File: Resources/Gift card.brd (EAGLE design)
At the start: 76.2 x 25.1 mm, 27 parts, among them J1 USBSMD, J2 LPC_SWD_PINPROG, Q1 IRLML6402, Q2 IRLML2502SOT23, U1 LPC11U24FBD48/301, U2 MMA8452Q, U3 NCP551SN33T1G, U4 NCP551SN50T1G, Y1 SMDCRYSTAL

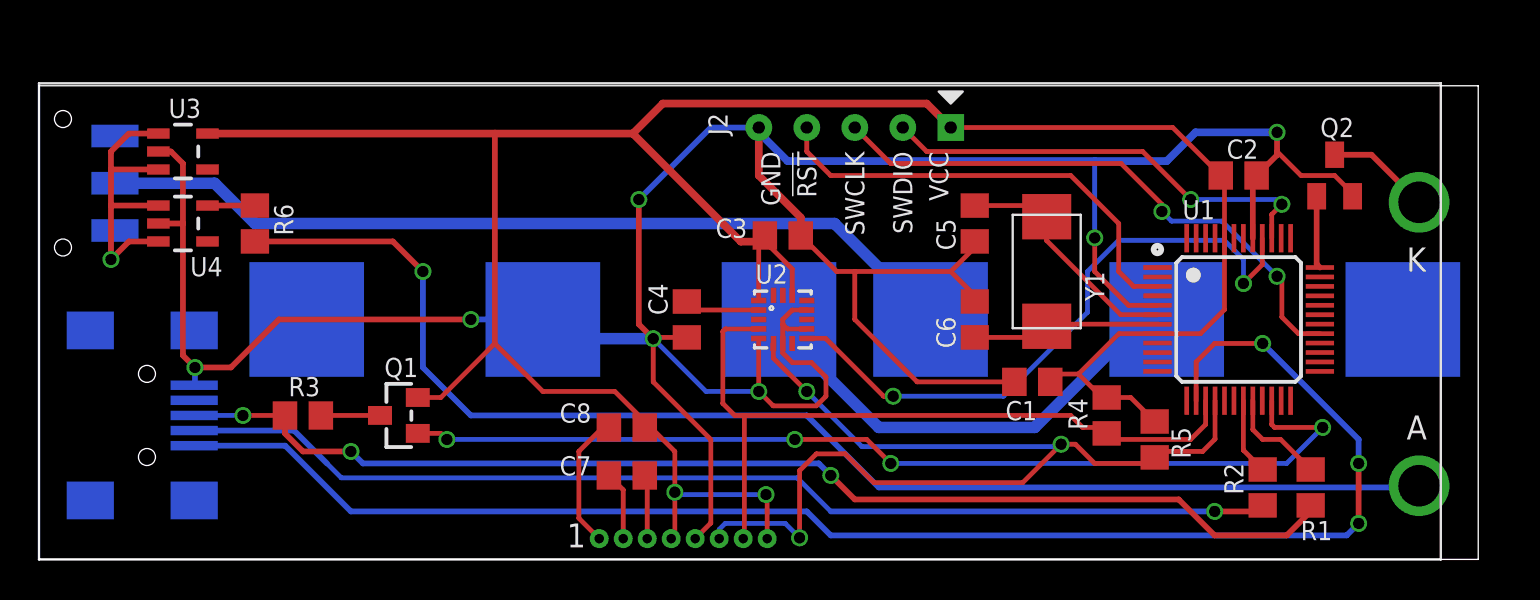
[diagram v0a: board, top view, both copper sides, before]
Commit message: Added drawable: hole; refactored abstraction error to #define
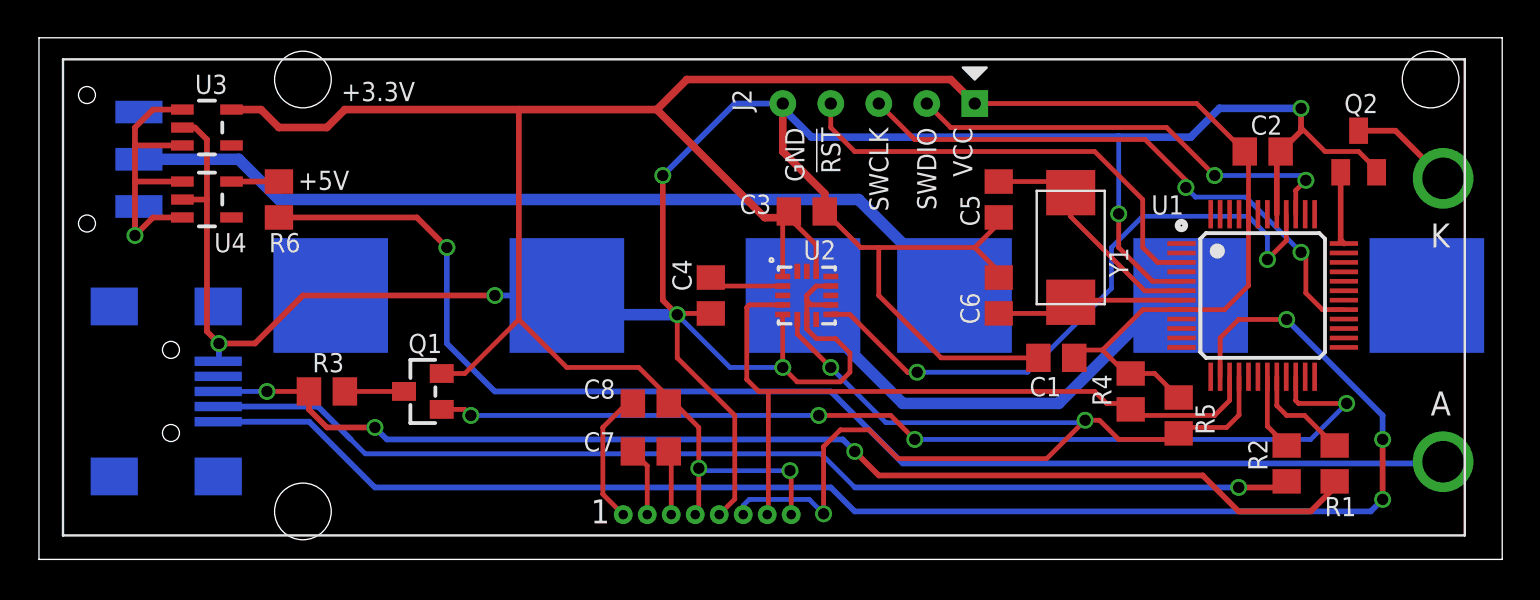
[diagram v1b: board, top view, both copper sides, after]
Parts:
- moved R2 1.80 mm to (66.0, 5.08)
- moved BT2 1.80 mm to (61.0, 14.0)
- moved C4 1.80 mm to (35.6, 14.0)
- moved U2 1.80 mm to (40.6, 14.0)
- moved R5 1.80 mm to (60.3, 7.62)
- moved C3 1.80 mm to (40.6, 18.4)
- moved J2 1.80 mm to (44.5, 24.1)
- moved J1 1.80 mm to (6.99, 8.89)
- moved BT1 1.80 mm to (27.9, 14.0)
- moved DS1 1.80 mm to (1.27, 1.27)
- moved C8 1.80 mm to (32.4, 8.26)
- moved Q1 1.80 mm to (20.3, 8.89)
- moved R3 1.80 mm to (15.2, 8.89)
- moved S1 1.80 mm to (2.54, 17.8)
- moved U3 1.80 mm to (8.89, 22.9)
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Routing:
- net 3V3: track 135.9 -> 136.7 mm
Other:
- board size 76.2 x 25.1 mm -> 77.5 x 27.6 mm
- board text added: "+3.3V"
- board text added: "+5V"
- board text added: "JWJ #2014-001"
- board text removed: "#2014-001"

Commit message: Fixed MR270 rotations for texts; fixed problem with non-attribute texts not being drawn
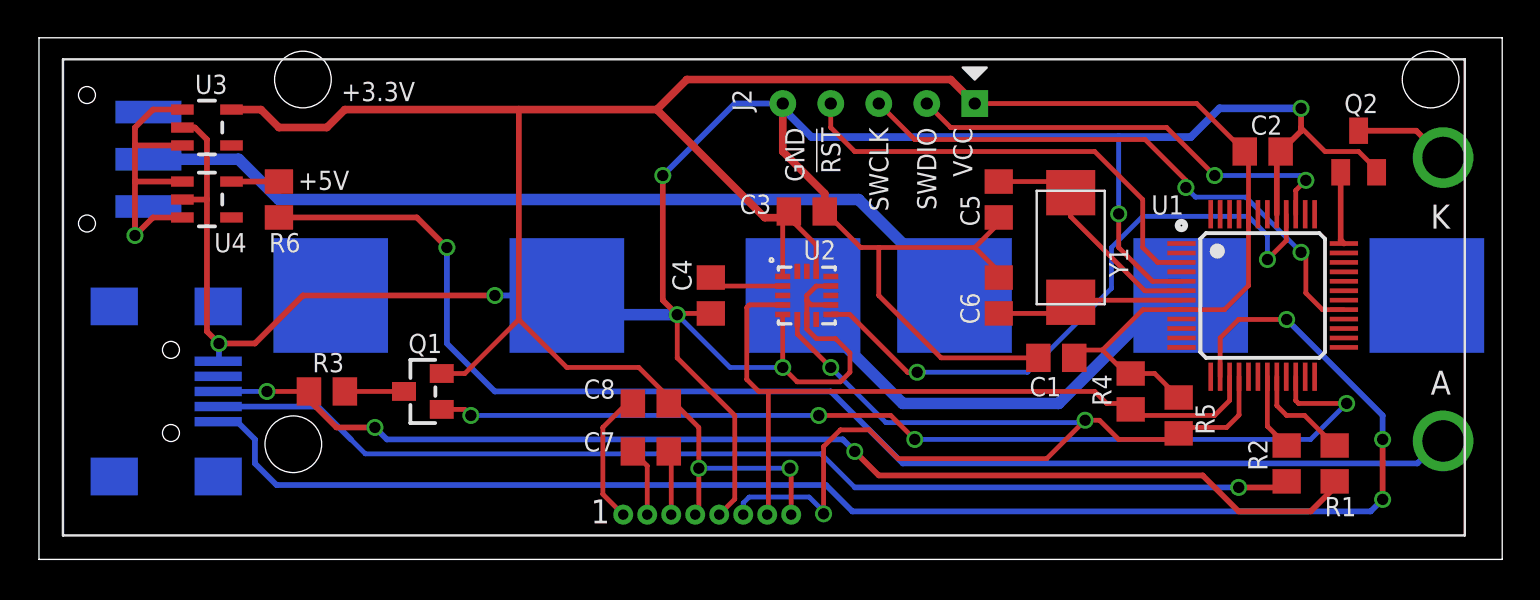
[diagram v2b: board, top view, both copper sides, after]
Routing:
- net PIO0_3: track 81.5 -> 82.2 mm
- net PIO0_5: track 53.5 -> 54.3 mm
- net VIN: track 18.3 -> 18.8 mm
- net N$11: track 46.2 -> 45.7 mm
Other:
- board text added: "!RST"
- board text added: "GND"
- board text added: "SWCLK"
- board text added: "SWDIO"
- board text added: "VCC"
